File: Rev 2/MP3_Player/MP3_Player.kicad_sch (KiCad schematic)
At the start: 28 parts, among them J1 AudioJack3_SwitchT, M1 Haptic Feedback, Q1 BS170, SW1 Home, SW2 Back, SW3 Play/Pause, SW4 Power, SW5 Menu, SW6 Hold, U1 Wemos Lolin32 Lite

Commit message: Added Flyback Diode
-Added Flyback Diode to prevent sparking and unwanted behavior
-Finished high power rails
-Fixed Screen Orientation
-Fixed Placement of some components
-Fixed Silkscreen
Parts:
- added D1: Flyback Diode, Diode_THT:D_A-405_P7.62mm_Horizontal, symbol Device:D
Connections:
- net GND: now also D1.2 (A)
- net at M1.1 (+), R7.2: now also D1.1 (K)
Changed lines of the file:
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@@
+	)
+	(junction
+		(at 243.84 129.54)
+		(diameter 0)
+		(color 0 0 0 0)
+	)
+	(junction
+		(at 243.84 116.84)
+		(diameter 0)
+		(color 0 0 0 0)
 	)
 	(junction
@@
 	(wire
 		(pts
+			(xy 223.52 118.11) (xy 223.52 116.84)
+		)
+		(stroke
+			(width 0)
+			(type default)
+		)
+	)
+	(wire
+		(pts
 			(xy 139.7 29.21) (xy 172.72 29.21)
 		)
@@
 	(wire
 		(pts
+			(xy 223.52 116.84) (xy 243.84 116.84)
+		)
+		(stroke
+			(width 0)
+			(type default)
+		)
+	)
+	(wire
+		(pts
 			(xy 66.04 156.21) (xy 77.47 156.21)
 		)
@@
 	(wire
 		(pts
+			(xy 223.52 125.73) (xy 223.52 129.54)
+		)
+		(stroke
+			(width 0)
+			(type default)
+		)
+	)
+	(wire
+		(pts
 			(xy 123.19 43.18) (xy 139.7 43.18)
 		)
@@
 		(pts
 			(xy 80.01 171.45) (xy 80.01 173.99)
+		)
+		(stroke
+			(width 0)
+			(type default)
+		)
+	)
+	(wire
+		(pts
+			(xy 223.52 129.54) (xy 243.84 129.54)
 		)
 		(stroke
@@
 					(unit 1)
 				)
+			)
+		)
+	)
+	(symbol
+		(lib_id "Device:D")
+		(at 223.52 121.92 270)
+		(unit 1)
+		(exclude_from_sim no)
+		(in_bom yes)
+		(on_board yes)
+		(dnp no)
+		(fields_autoplaced yes)
+		(property "Reference" "D1"
+			(at 226.06 120.6499 90)
+			(effects
+				(font
+					(size 1.27 1.27)
+				)
+				(justify left)
+			)
+		)
+		(property "Value" "Flyback Diode"
+			(at 226.06 123.1899 90)
+			(effects
+				(font
+					(size 1.27 1.27)
+				)
+				(justify left)
+			)
+		)
+		(property "Footprint" "Diode_THT:D_A-405_P7.62mm_Horizontal"
+			(at 223.52 121.92 0)
+			(effects
+				(font
+					(size 1.27 1.27)
+				)
+				(hide yes)
+			)
+		)
+		(property "Datasheet" "~"
+			(at 223.52 121.92 0)
+			(effects
+				(font
+					(size 1.27 1.27)
+				)
+				(hide yes)
+			)
+		)
+		(property "Description" "Diode"
+			(at 223.52 121.92 0)
+			(effects
+				(font
+					(size 1.27 1.27)
+				)
+				(hide yes)
+			)
+		)
+		(property "Sim.Device" "D"
+			(at 223.52 121.92 0)
+			(effects
+				(font
+					(size 1.27 1.27)
+				)
+				(hide yes)
+			)
+		)
+		(property "Sim.Pins" "1=K 2=A"
+			(at 223.52 121.92 0)
+			(effects
+				(font
+					(size 1.27 1.27)
+				)
+				(hide yes)
+			)
+		)
+		(pin "1"
+		)
+		(pin "2"
+		)
+		(instances
+			(project ""
+				(path "/caa12bce-cf4c-4041-a9a3-d1ebb8f4f00b"
+					(reference "D1")
+					(unit 1)
+				)

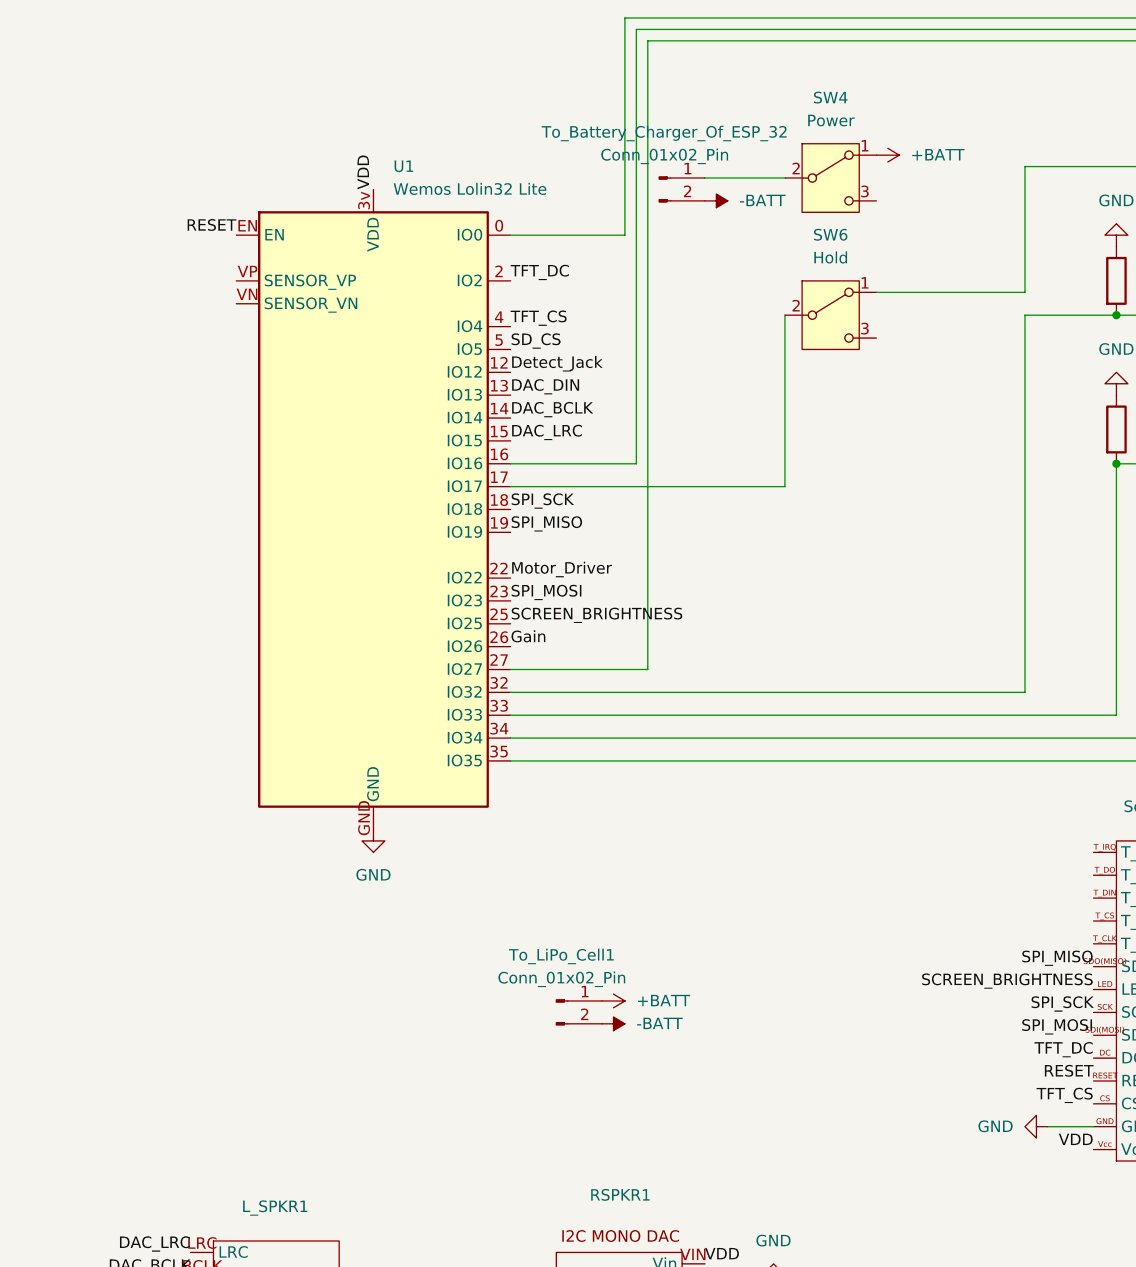
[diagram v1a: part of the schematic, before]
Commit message: Finished routing PCB
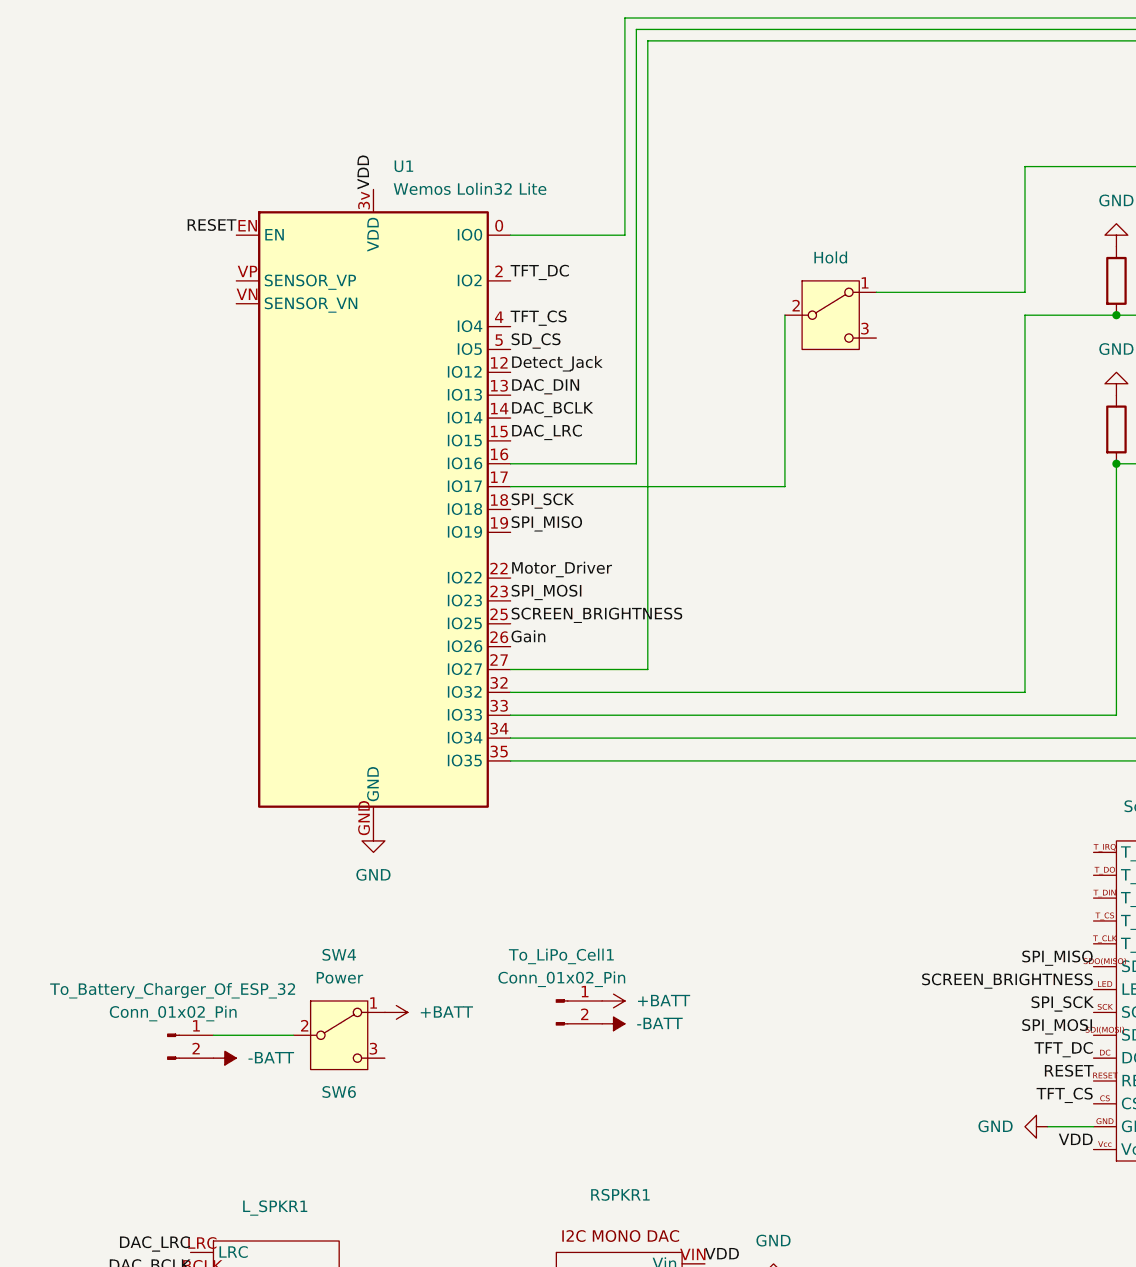
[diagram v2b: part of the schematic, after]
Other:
- moved on the sheet: SW4, To_Battery_Charger_Of_ESP_32
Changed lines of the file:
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@@
 	(wire
 		(pts
-			(xy 104.14 30.48) (xy 113.03 30.48)
-		)
-		(stroke
-			(width 0)
-			(type default)
-		)
-	)
-	(wire
-		(pts
 			(xy 172.72 29.21) (xy 172.72 45.72)
 		)
@@
 	(wire
 		(pts
+			(xy 49.53 125.73) (xy 58.42 125.73)
+		)
+		(stroke
+			(width 0)
+			(type default)
+		)
+	)
+	(wire
+		(pts
 			(xy 160.02 68.58) (xy 160.02 92.71)
 		)
@@
 	(symbol
 		(lib_id "power:+BATT")
-		(at 123.19 27.94 270)
+		(at 68.58 123.19 270)
 		(unit 1)
 		(exclude_from_sim no)
@@
 		(fields_autoplaced yes)
 		(property "Reference" "#PWR06"
-			(at 119.38 27.94 0)
+			(at 64.77 123.19 0)
 			(effects
 				(font
@@
 		)
 		(property "Value" "+BATT"
-			(at 127 27.9399 90)
+			(at 72.39 123.1899 90)
 			(effects
 				(font
@@
 		)
 		(property "Footprint" ""
-			(at 123.19 27.94 0)
+			(at 68.58 123.19 0)
 			(effects
 				(font
@@
 		)
 		(property "Datasheet" ""
-			(at 123.19 27.94 0)
+			(at 68.58 123.19 0)
 			(effects
 				(font
@@
 		)
 		(property "Description" "Power symbol creates a global label with name \"+BATT\""
-			(at 123.19 27.94 0)
+			(at 68.58 123.19 0)
 			(effects
 				(font
@@
 	(symbol
 		(lib_id "Connector:Conn_01x02_Pin")
-		(at 99.06 30.48 0)
+		(at 44.45 125.73 0)
 		(unit 1)
 		(exclude_from_sim no)
@@
 		(fields_autoplaced yes)
 		(property "Reference" "To_Battery_Charger_Of_ESP_32"
-			(at 99.695 25.4 0)
+			(at 45.085 120.65 0)
 			(effects
 				(font
@@
 		)
 		(property "Value" "Conn_01x02_Pin"
-			(at 99.695 27.94 0)
+			(at 45.085 123.19 0)
 			(effects
 				(font
@@
 		)
 		(property "Footprint" "Connector_JST:JST_XA_B02B-XASK-1-A_1x02_P2.50mm_Vertical"
-			(at 99.06 30.48 0)
+			(at 44.45 125.73 0)
 			(effects
 				(font
@@
 		)
 		(property "Datasheet" "~"
-			(at 99.06 30.48 0)
+			(at 44.45 125.73 0)
 			(effects
 				(font
@@
 		)
 		(property "Description" "Generic connector, single row, 01x02, script generated"
-			(at 99.06 30.48 0)
+			(at 44.45 125.73 0)
 			(effects
 				(font
@@
 		(on_board yes)
 		(dnp no)
-		(fields_autoplaced yes)
 		(property "Reference" "SW6"
-			(at 118.11 36.83 0)
+			(at 63.5 132.08 0)
 			(effects
 				(font
@@
 	(symbol
 		(lib_id "power:-BATT")
-		(at 104.14 33.02 270)
+		(at 49.53 128.27 270)
 		(unit 1)
 		(exclude_from_sim no)
@@
 		(fields_autoplaced yes)
 		(property "Reference" "#PWR015"
-			(at 100.33 33.02 0)
+			(at 45.72 128.27 0)
 			(effects
 				(font
@@
 		)
 		(property "Value" "-BATT"
-			(at 107.95 33.0199 90)
+			(at 53.34 128.2699 90)
 			(effects
 				(font
@@
 		)
 		(property "Footprint" ""
-			(at 104.14 33.02 0)
+			(at 49.53 128.27 0)
 			(effects
 				(font
@@
 		)
 		(property "Datasheet" ""
-			(at 104.14 33.02 0)
+			(at 49.53 128.27 0)
 			(effects
 				(font
@@
 		)
 		(property "Description" "Power symbol creates a global label with name \"-BATT\""
-			(at 104.14 33.02 0)
+			(at 49.53 128.27 0)
 			(effects
 				(font
@@
 	(symbol
 		(lib_id "Switch:SW_SPDT")
-		(at 118.11 30.48 0)
+		(at 63.5 125.73 0)
 		(unit 1)
 		(exclude_from_sim no)
@@
 		(fields_autoplaced yes)
 		(property "Reference" "SW4"
-			(at 118.11 21.59 0)
+			(at 63.5 116.84 0)
 			(effects
 				(font
@@
 		)
 		(property "Value" "Power"
-			(at 118.11 24.13 0)
+			(at 63.5 119.38 0)
 			(effects
 				(font
@@
 		)
 		(property "Footprint" "Button_Switch_THT:SW_Slide_SPDT_Angled_CK_OS102011MA1Q"
-			(at 118.11 30.48 0)
+			(at 63.5 125.73 0)
 			(effects
 				(font
@@
 		)
 		(property "Datasheet" "~"
-			(at 118.11 38.1 0)
+			(at 63.5 133.35 0)
 			(effects
 				(font
@@
 		)
 		(property "Description" "Switch, single pole double throw"
-			(at 118.11 30.48 0)
+			(at 63.5 125.73 0)
 			(effects
 				(font
